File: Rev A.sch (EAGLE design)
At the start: 92 parts, among them IC101 LM833N, IC102 LM833N, Q101 2N3906, Q102 2N3906, Q103 2N3904, Q104 2N3904, Q105 2N3904, Q106 2N3904, Q107 2N3906, Q108 2N3906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

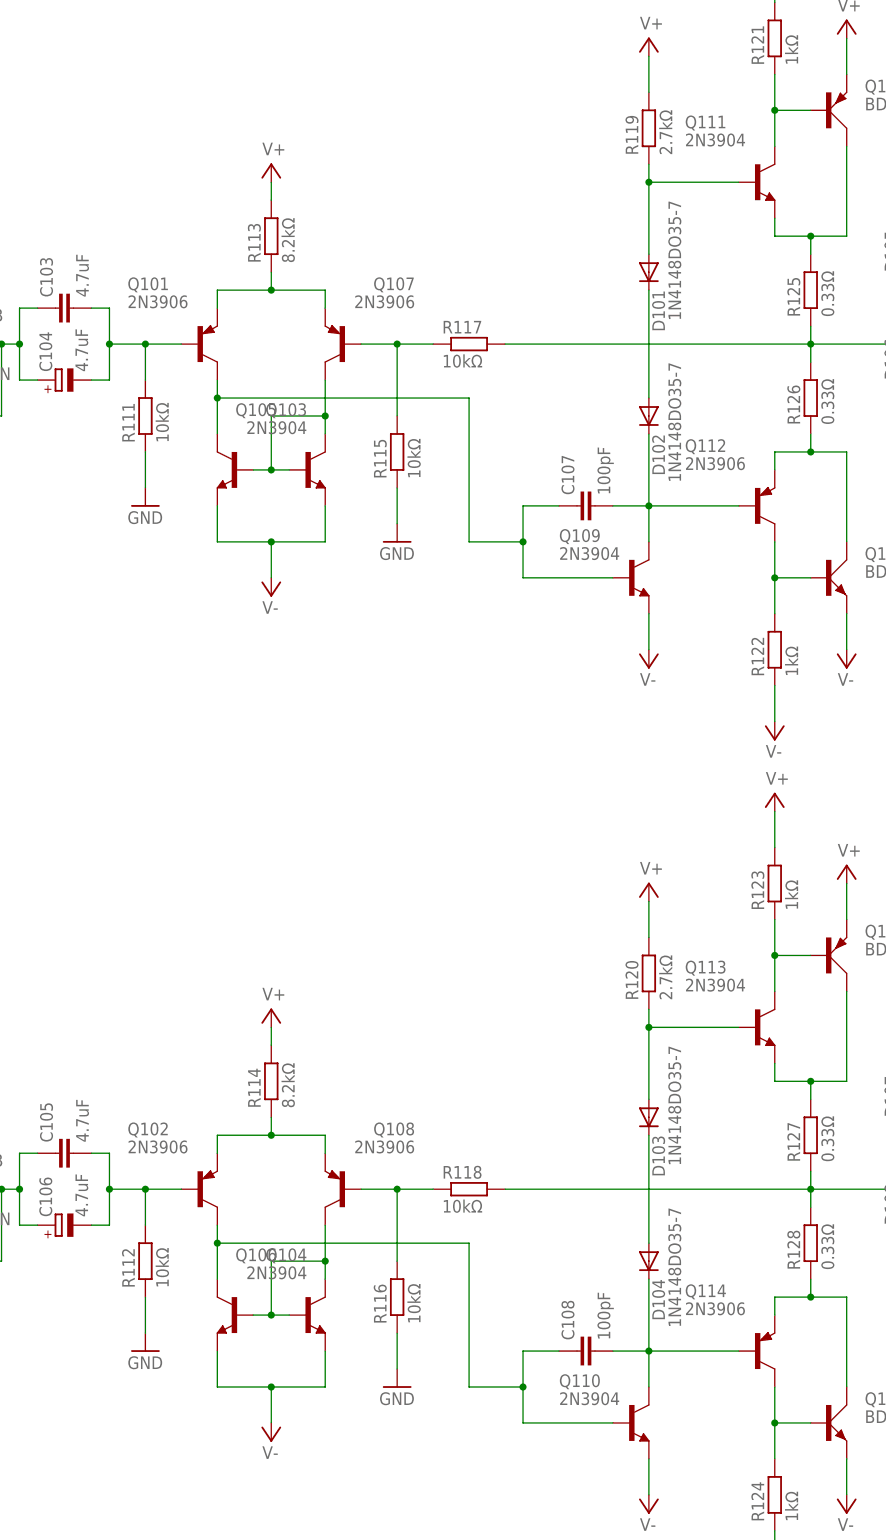
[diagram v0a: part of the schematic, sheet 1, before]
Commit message: Replaced all the low-power transistors with TO-18 versions
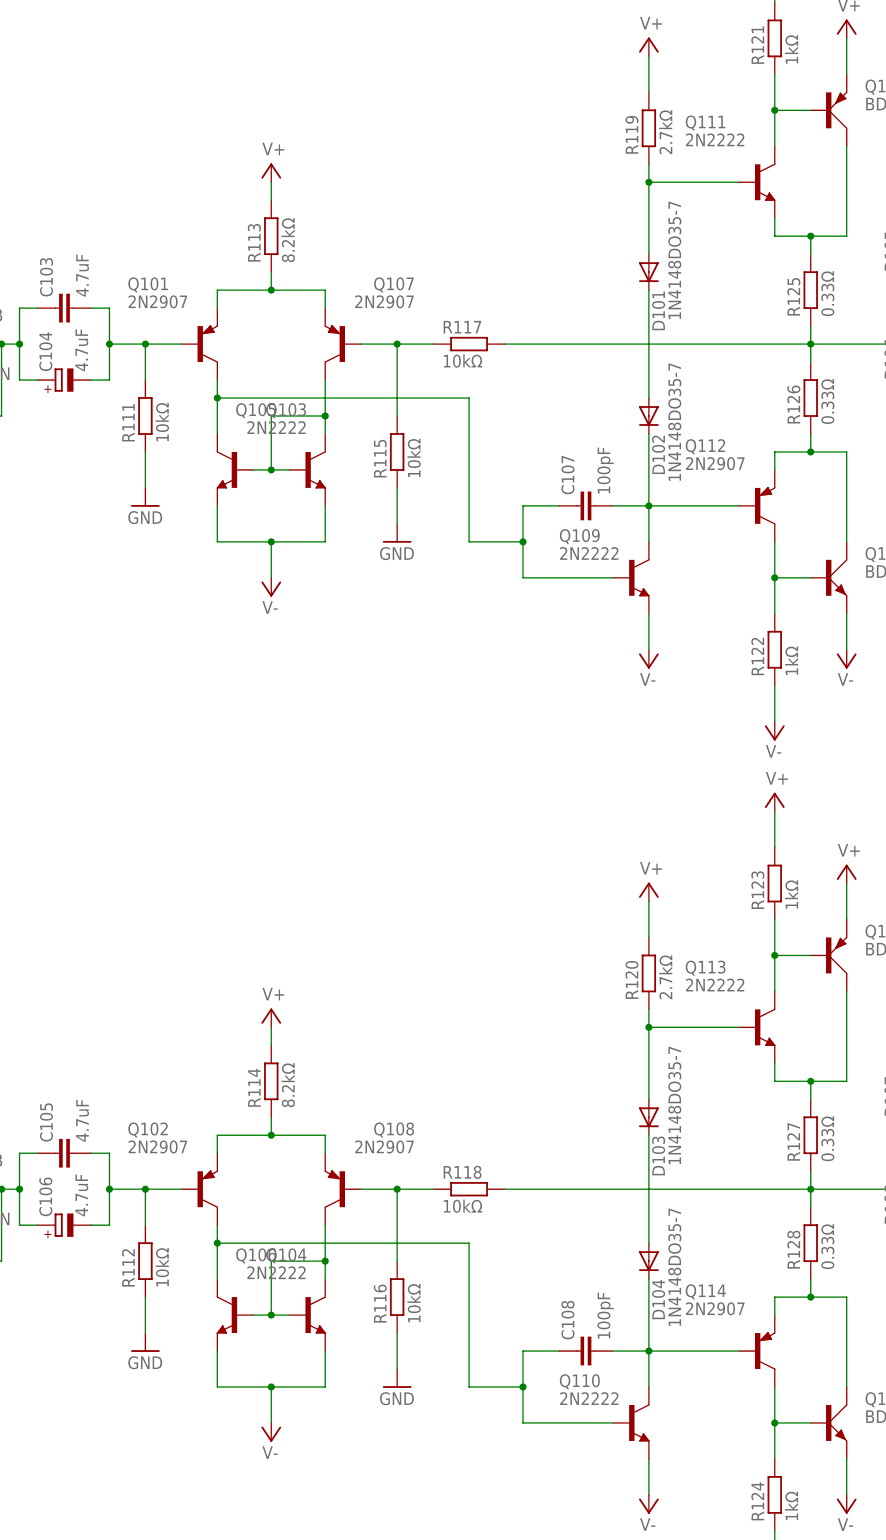
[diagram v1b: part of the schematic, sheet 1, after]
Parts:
- Q101, Q102, Q107, Q108, Q112, Q114: value 2N3906 -> 2N2907; device transistor-pnp:2N3906 -> transistor-pnp:2N2907
- Q103, Q104, Q105, Q106, Q109, Q110, Q111, Q113: value 2N3904 -> 2N2222; device transistor-npn:2N3904 -> transistor:2N2222

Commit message: Ready for production
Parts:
- removed C103, C105: 4.7uF, rcl:C-EU225-113X268
- removed H201, H202, H203, H204: MOUNT-HOLE3.0, holes:MOUNT-HOLE3.0
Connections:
- net N$25: no longer C105.2
- net N$30: no longer C105.1
- net N$5: no longer C103.2
- net N$6: no longer C103.1
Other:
- moved on the sheet: C104, C106
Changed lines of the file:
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@@
 <part name="SUPPLY18" library="supply2" deviceset="V-" device=""/>
 <part name="C107" library="rcl" deviceset="C-EU" device="050-050X075" value="100pF"/>
-<part name="C103" library="rcl" deviceset="C-EU" device="225-113X268" value="4.7uF"/>
 <part name="C104" library="rcl" deviceset="CPOL-EU" device="E2-5" value="4.7uF"/>
 <part name="Q101" library="transistor-pnp" deviceset="2N2907*" device=""/>
@@
 <part name="SUPPLY36" library="supply2" deviceset="V-" device=""/>
 <part name="C108" library="rcl" deviceset="C-EU" device="050-050X075" value="100pF"/>
-<part name="C105" library="rcl" deviceset="C-EU" device="225-113X268" value="4.7uF"/>
 <part name="C106" library="rcl" deviceset="CPOL-EU" device="E2-5" value="4.7uF"/>
 <part name="Q102" library="transistor-pnp" deviceset="2N2907*" device=""/>
@@
 <part name="SWT_IN" library="adafruit" deviceset="JST_2PIN" device="-THM"/>
 <part name="SUPPLY60" library="supply2" deviceset="V-" device=""/>
-<part name="H201" library="holes" deviceset="MOUNT-HOLE" device="3.0"/>
-<part name="H202" library="holes" deviceset="MOUNT-HOLE" device="3.0"/>
-<part name="H203" library="holes" deviceset="MOUNT-HOLE" device="3.0"/>
-<part name="H204" library="holes" deviceset="MOUNT-HOLE" device="3.0"/>
 <part name="SUPPLY7" library="supply2" deviceset="V-" device=""/>
 <part name="GND3" library="supply1" deviceset="GND" device=""/>
@@
 <instance part="SUPPLY18" gate="1" x="165.1" y="53.34"/>
 <instance part="C107" gate="G$1" x="119.38" y="48.26" rot="R90"/>
-<instance part="C103" gate="G$1" x="45.72" y="76.2" rot="R90"/>
-<instance part="C104" gate="G$1" x="45.72" y="66.04" rot="R90"/>
+<instance part="C104" gate="G$1" x="45.72" y="71.12" rot="R90"/>
 <instance part="Q101" gate="G$1" x="66.04" y="71.12"/>
 <instance part="Q107" gate="G$1" x="86.36" y="71.12" rot="MR0"/>
@@
 <instance part="SUPPLY36" gate="1" x="165.1" y="-66.04"/>
 <instance part="C108" gate="G$1" x="119.38" y="-71.12" rot="R90"/>
-<instance part="C105" gate="G$1" x="45.72" y="-43.18" rot="R90"/>
-<instance part="C106" gate="G$1" x="45.72" y="-53.34" rot="R90"/>
+<instance part="C106" gate="G$1" x="45.72" y="-48.26" rot="R90"/>
 <instance part="Q102" gate="G$1" x="66.04" y="-48.26"/>
 <instance part="Q108" gate="G$1" x="86.36" y="-48.26" rot="MR0"/>
@@
 <segment>
 <pinref part="C104" gate="G$1" pin="-"/>
-<wire x1="50.8" y1="66.04" x2="53.34" y2="66.04" width="0.1524" layer="91"/>
-<wire x1="53.34" y1="66.04" x2="53.34" y2="71.12" width="0.1524" layer="91"/>
-<pinref part="C103" gate="G$1" pin="2"/>
-<wire x1="53.34" y1="71.12" x2="53.34" y2="76.2" width="0.1524" layer="91"/>
-<wire x1="53.34" y1="76.2" x2="50.8" y2="76.2" width="0.1524" layer="91"/>
 <pinref part="Q101" gate="G$1" pin="B"/>
-<wire x1="53.34" y1="71.12" x2="58.42" y2="71.12" width="0.1524" layer="91"/>
+<wire x1="50.8" y1="71.12" x2="58.42" y2="71.12" width="0.1524" layer="91"/>
 <pinref part="R111" gate="G$1" pin="2"/>
 <wire x1="58.42" y1="71.12" x2="63.5" y2="71.12" width="0.1524" layer="91"/>
 <wire x1="58.42" y1="66.04" x2="58.42" y2="71.12" width="0.1524" layer="91"/>
 <junction x="58.42" y="71.12"/>
-<junction x="53.34" y="71.12"/>
 </segment>
 </net>
 <net name="N$6" class="0">
 <segment>
-<pinref part="C103" gate="G$1" pin="1"/>
-<wire x1="43.18" y1="76.2" x2="40.64" y2="76.2" width="0.1524" layer="91"/>
 <pinref part="C104" gate="G$1" pin="+"/>
-<wire x1="40.64" y1="76.2" x2="40.64" y2="71.12" width="0.1524" layer="91"/>
-<wire x1="40.64" y1="71.12" x2="40.64" y2="66.04" width="0.1524" layer="91"/>
-<wire x1="40.64" y1="66.04" x2="43.18" y2="66.04" width="0.1524" layer="91"/>
 <pinref part="R109" gate="G$1" pin="2"/>
 <wire x1="33.02" y1="60.96" x2="38.1" y2="60.96" width="0.1524" layer="91"/>
 <wire x1="38.1" y1="60.96" x2="38.1" y2="71.12" width="0.1524" layer="91"/>
 <wire x1="35.56" y1="71.12" x2="38.1" y2="71.12" width="0.1524" layer="91"/>
-<wire x1="38.1" y1="71.12" x2="40.64" y2="71.12" width="0.1524" layer="91"/>
+<wire x1="38.1" y1="71.12" x2="43.18" y2="71.12" width="0.1524" layer="91"/>
 <junction x="38.1" y="71.12"/>
 <pinref part="IC101" gate="B" pin="OUT"/>
-<junction x="40.64" y="71.12"/>
 </segment>
 </net>
@@
 <segment>
 <pinref part="C106" gate="G$1" pin="-"/>
-<wire x1="50.8" y1="-53.34" x2="53.34" y2="-53.34" width="0.1524" layer="91"/>
-<wire x1="53.34" y1="-53.34" x2="53.34" y2="-48.26" width="0.1524" layer="91"/>
-<pinref part="C105" gate="G$1" pin="2"/>
-<wire x1="53.34" y1="-48.26" x2="53.34" y2="-43.18" width="0.1524" layer="91"/>
-<wire x1="53.34" y1="-43.18" x2="50.8" y2="-43.18" width="0.1524" layer="91"/>
 <pinref part="Q102" gate="G$1" pin="B"/>
-<wire x1="53.34" y1="-48.26" x2="58.42" y2="-48.26" width="0.1524" layer="91"/>
+<wire x1="50.8" y1="-48.26" x2="58.42" y2="-48.26" width="0.1524" layer="91"/>
 <pinref part="R112" gate="G$1" pin="2"/>
 <wire x1="58.42" y1="-48.26" x2="63.5" y2="-48.26" width="0.1524" layer="91"/>
 <wire x1="58.42" y1="-53.34" x2="58.42" y2="-48.26" width="0.1524" layer="91"/>
 <junction x="58.42" y="-48.26"/>
-<junction x="53.34" y="-48.26"/>
 </segment>
 </net>
 <net name="N$30" class="0">
 <segment>
-<pinref part="C105" gate="G$1" pin="1"/>
-<wire x1="43.18" y1="-43.18" x2="40.64" y2="-43.18" width="0.1524" layer="91"/>
 <pinref part="C106" gate="G$1" pin="+"/>
-<wire x1="40.64" y1="-43.18" x2="40.64" y2="-48.26" width="0.1524" layer="91"/>
-<wire x1="40.64" y1="-48.26" x2="40.64" y2="-53.34" width="0.1524" layer="91"/>
-<wire x1="40.64" y1="-53.34" x2="43.18" y2="-53.34" width="0.1524" layer="91"/>
 <pinref part="R110" gate="G$1" pin="2"/>
 <wire x1="33.02" y1="-58.42" x2="38.1" y2="-58.42" width="0.1524" layer="91"/>
 <wire x1="38.1" y1="-58.42" x2="38.1" y2="-48.26" width="0.1524" layer="91"/>
 <wire x1="35.56" y1="-48.26" x2="38.1" y2="-48.26" width="0.1524" layer="91"/>
-<wire x1="38.1" y1="-48.26" x2="40.64" y2="-48.26" width="0.1524" layer="91"/>
+<wire x1="38.1" y1="-48.26" x2="43.18" y2="-48.26" width="0.1524" layer="91"/>
 <junction x="38.1" y="-48.26"/>
 <pinref part="IC102" gate="B" pin="OUT"/>
-<junction x="40.64" y="-48.26"/>
 </segment>
 </net>
@@
 <instance part="SWT_IN" gate="G$1" x="10.16" y="76.2" rot="R180"/>
 <instance part="SUPPLY60" gate="1" x="124.46" y="15.24"/>
-<instance part="H201" gate="G$1" x="81.28" y="86.36"/>
-<instance part="H202" gate="G$1" x="81.28" y="78.74"/>
-<instance part="H203" gate="G$1" x="81.28" y="71.12"/>
-<instance part="H204" gate="G$1" x="81.28" y="63.5"/>
 <instance part="SUPPLY7" gate="1" x="33.02" y="60.96"/>
 <instance part="GND3" gate="1" x="48.26" y="60.96"/>
